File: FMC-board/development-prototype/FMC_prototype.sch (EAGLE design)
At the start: 3 parts

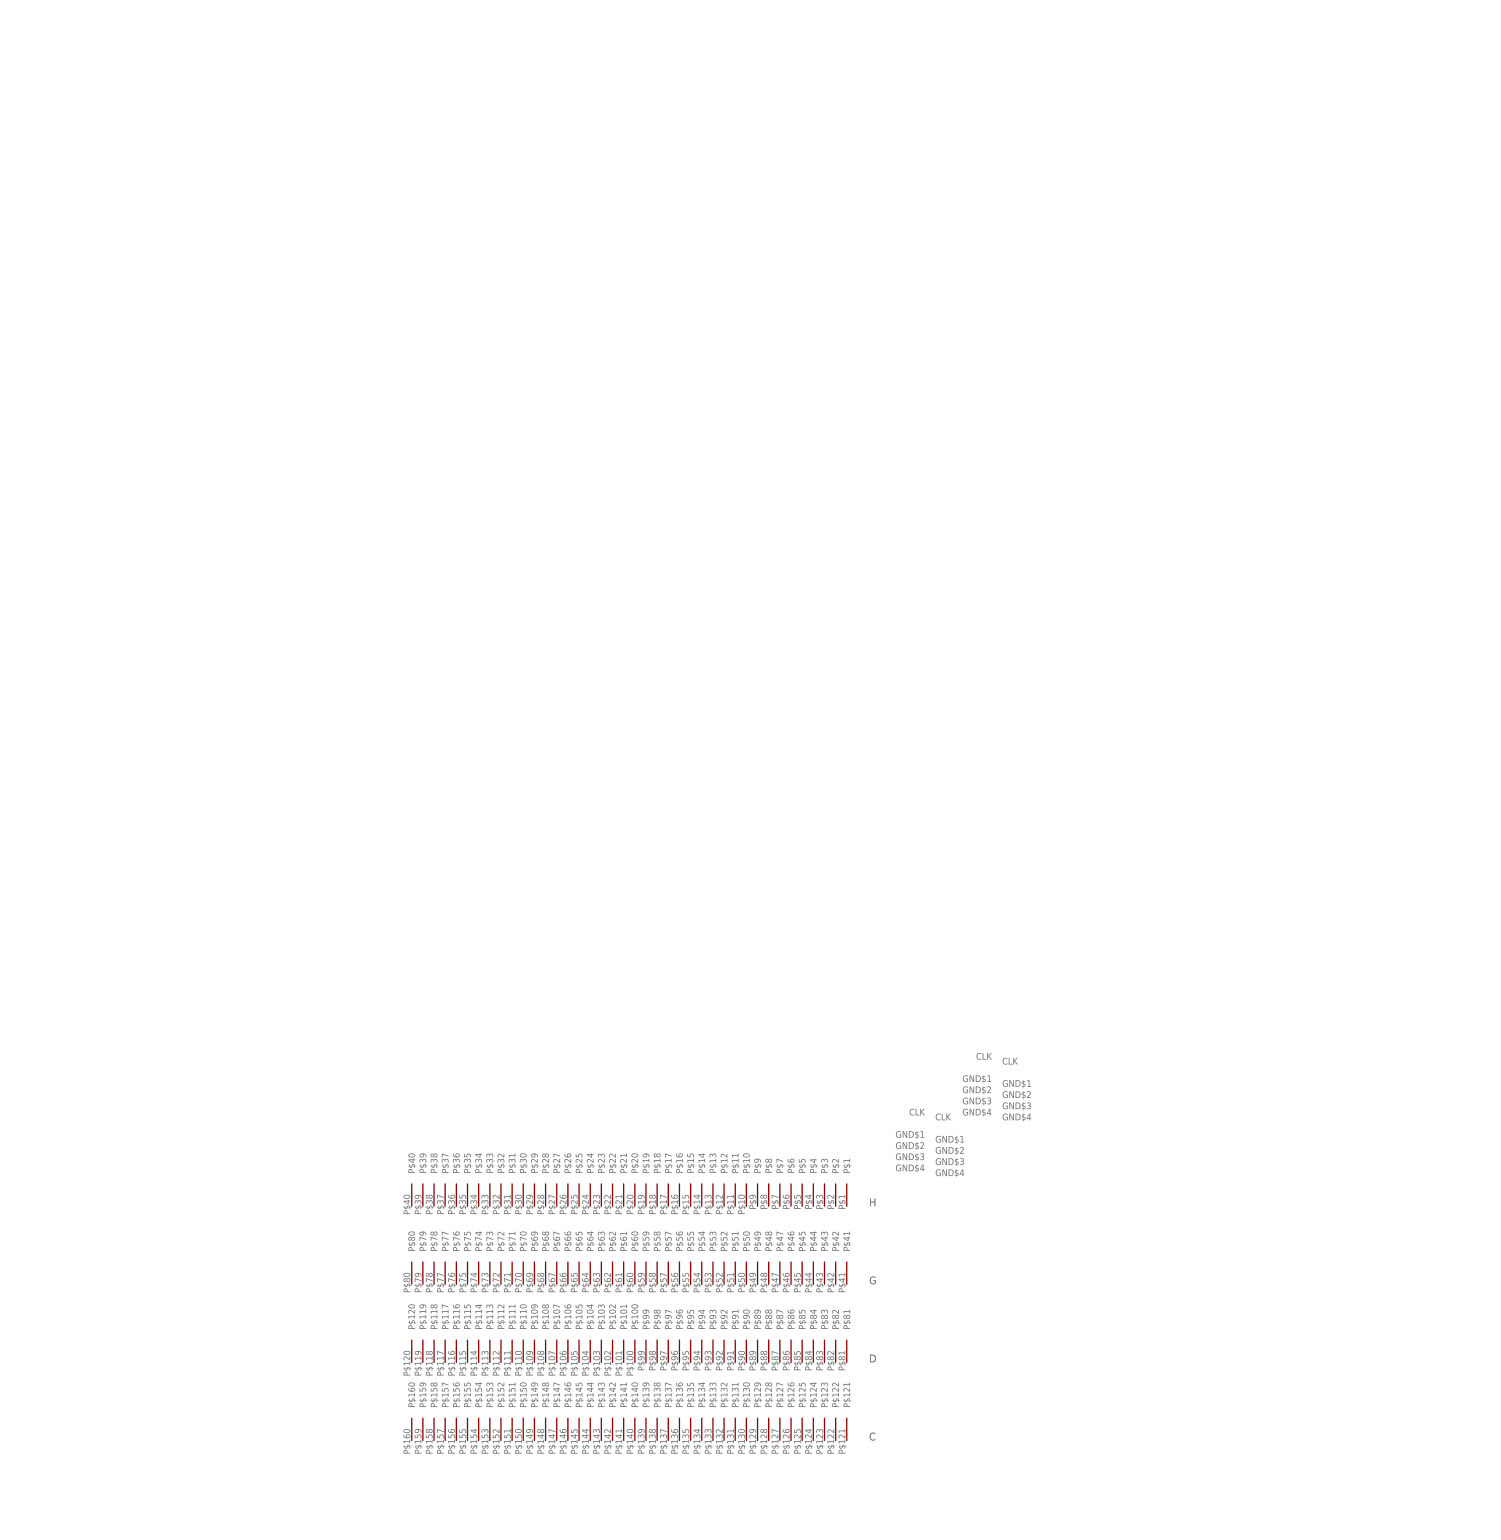
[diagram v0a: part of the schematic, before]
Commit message: added basic isolator circuitry sch
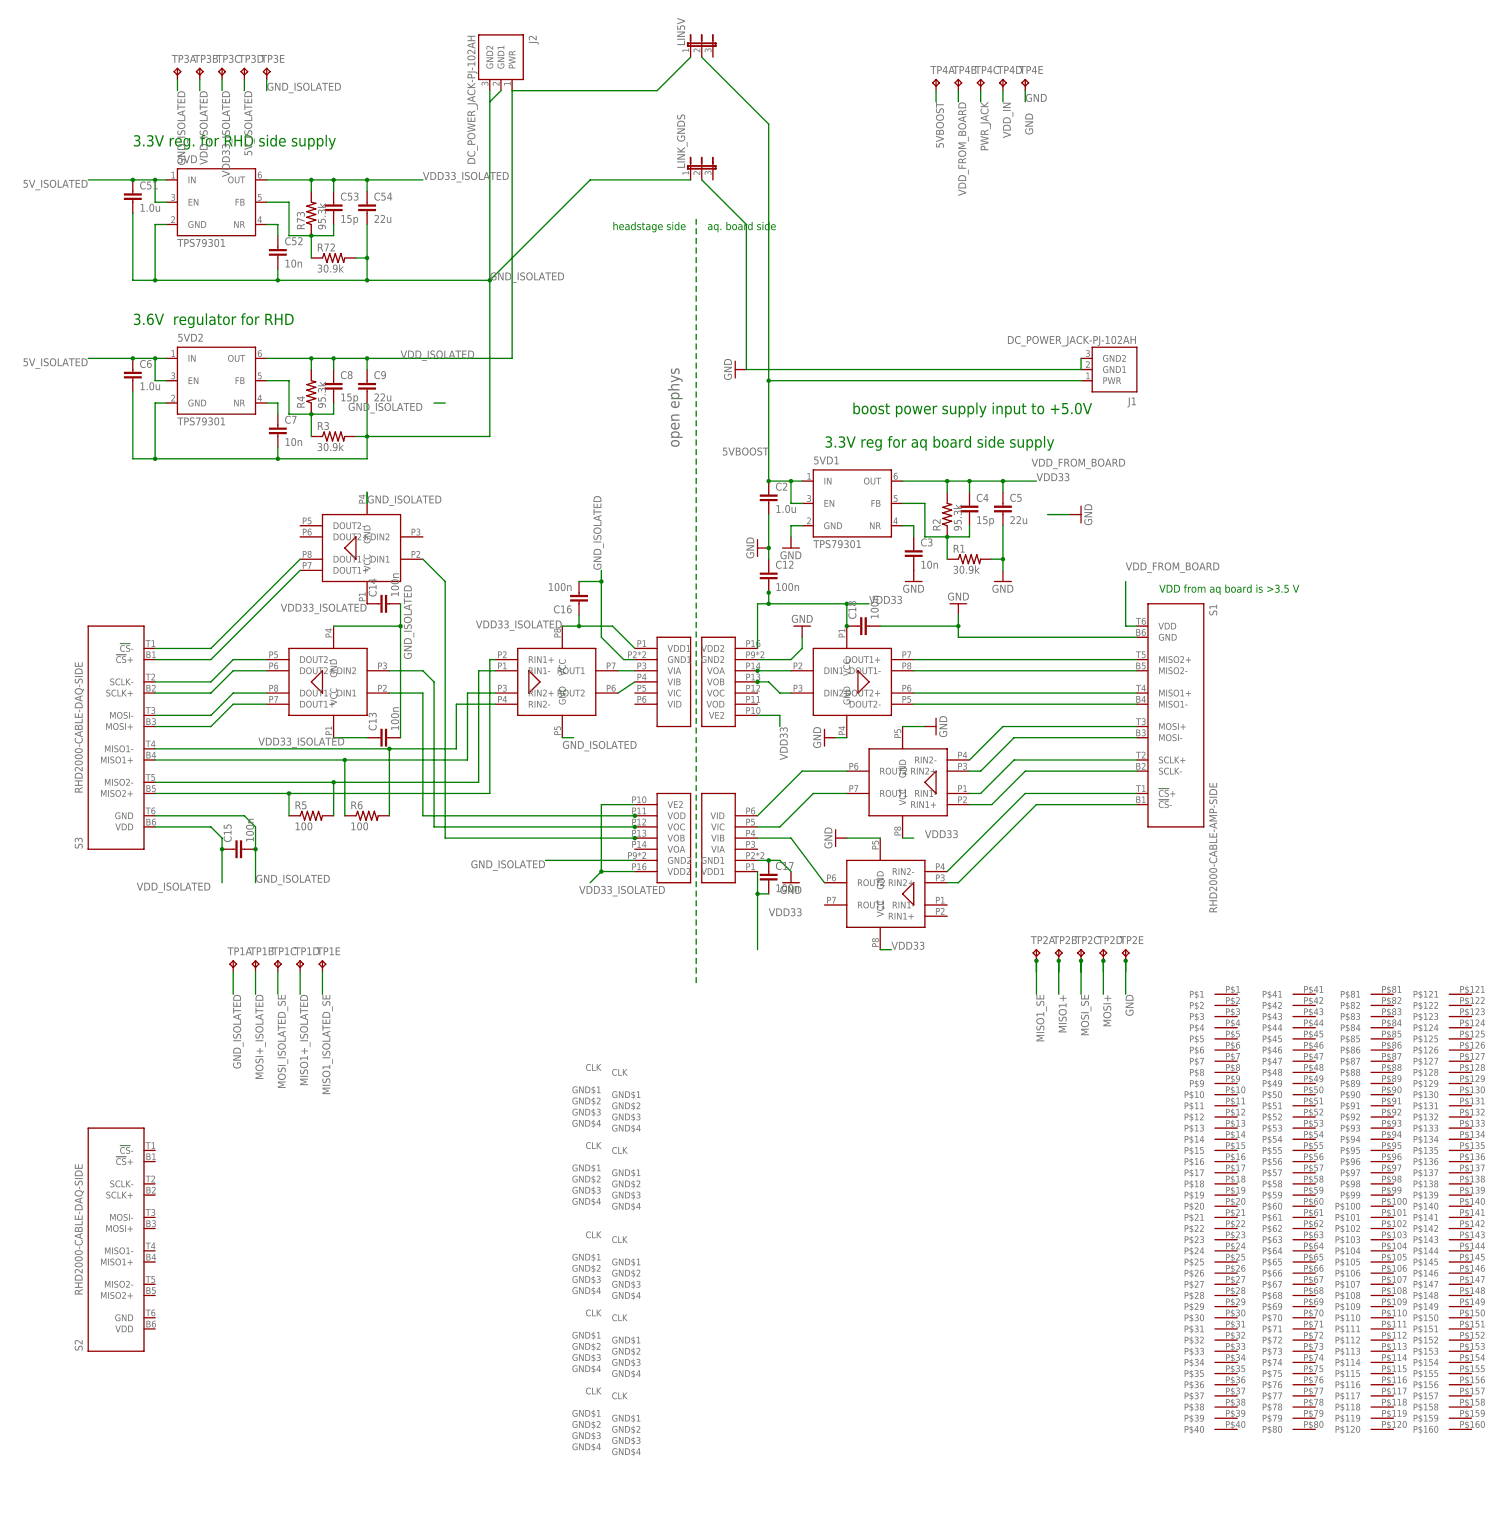
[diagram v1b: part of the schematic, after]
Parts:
- added 5VD, 5VD1, 5VD2: TPS79301, RHD2000_eval_board:TPS79301
- added C12, C13, C14, C15, C16, C17, C18: 100n, RHD2000_eval_board:C_0603
- added C2, C51, C6: 1.0u, RHD2000_eval_board:C_0805
- added C3, C52, C7: 10n, RHD2000_eval_board:C_0603
- added C4, C53, C8: 15p, RHD2000_eval_board:C_0603
- added C5, C54, C9: 22u, RHD2000_eval_board:C_1206
- added J1, J2: DC_POWER_JACK-PJ-102AH, RHD2000_eval_board:DC_POWER_JACK-PJ-102AH
- added LIN5V, LINK_GNDS: (no value), jumper:JP2E
- added R1, R3, R72: 30.9k, RHD2000_eval_board:R_0603
- added R2, R4, R73: 95.3k, RHD2000_eval_board:R_0603
- added R5, R6: 100, RHD2000_eval_board:R_0603
- added S1: RHD2000-CABLE-AMP-SIDE, RHD2000:RHD2000-CABLE-AMP-SIDE
- added S2, S3: RHD2000-CABLE-DAQ-SIDE, RHD2000_eval_board:RHD2000-CABLE-DAQ-SIDE
- added TP1, TP2, TP3, TP4: TP5P5-25-13, testpad:TP5P5-25-13
- added U$1: OPEN_EPHYS_LOGO, open-ephys:OPEN_EPHYS_LOGO
- added U$10, U$6, U$8: ADN4664, open-ephys:ADN4664
- added U$11, U$12: ADUM3440, open-ephys_old:ADUM3440
- added U$13, U$14, U$15: SMA_JACK_142-0701-201_DEV, SA_BB:SMA_JACK_142-0701-201_DEV
- added U$3, U$7, U$9: ADN4663, open-ephys:ADN4663
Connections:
- new net 5VBOOST: 5VD1.EN, 5VD1.IN, C2.1, J1.PWR, LIN5V.2, TP4A.TP
- new net 5V_ISOLATED: 5VD.EN, 5VD.IN, 5VD2.EN, 5VD2.IN, C51.1, C6.1, TP3D.TP
- new net CS+: S1.!CS!+, U$10.RIN2-
- new net CS+_ISOLATED: S3.!CS!+, U$9.DOUT1+
- new net CS-: S1.!CS!-, U$10.RIN2+
- new net CS-_ISOLATED: S3.!CS!-, U$9.DOUT1-
- new net CS_ISOLATED_SE: U$12.VOB, U$9.DIN1
- new net CS_SE: U$10.ROUT2, U$12.VIB
- new net GND: 5VD1.GND, C12.1, C17.1, C18.2, C2.2, C3.2, C5.2, J1.GND1, J1.GND2, LINK_GNDS.2, R1.2, S1.GND, TP2E.TP, TP4E.TP, U$10.GND, U$11.GND2, U$12.GND1, U$3.GND, U$8.GND
- new net GND4: C15.2
- new net GND_ISOLATED: 5VD.GND, 5VD2.GND, C13.2, C14.2, C16.2, C51.2, C52.2, C54.2, C6.2, C7.2, C9.2, J2.GND1, J2.GND2, LINK_GNDS.1, R3.2, R72.2, S3.GND, TP1A.TP, TP3A.TP, TP3E.TP, U$11.GND1, U$12.GND2, U$6.GND, U$7.GND, U$9.GND
- new net MISO1+: S1.MISO1+, TP2B.TP, U$3.DOUT2+
- new net MISO1+_ISOLATED: R6.1, S3.MISO1+, TP1D.TP, U$6.RIN2+
- new net MISO1-: S1.MISO1-, U$3.DOUT2-
- new net MISO1-_ISOLATED: R6.2, S3.MISO1-, U$6.RIN2-
- new net MISO1_ISOLATED_SE: TP1E.TP, U$11.VIB, U$6.ROUT2
- new net MISO1_SE: TP2A.TP, U$11.VOB, U$3.DIN2
- new net MISO2+: S1.MISO2+, U$3.DOUT1+
- new net MISO2+_ISOLATED: R5.1, S3.MISO2+, U$6.RIN1+
- new net MISO2-: S1.MISO2-, U$3.DOUT1-
- new net MISO2-_ISOLATED: R5.2, S3.MISO2-, U$6.RIN1-
- new net MISO2_ISOLATED_SE: U$11.VIA, U$6.ROUT1
- new net MISO2_SE: U$11.VOA, U$3.DIN1
- new net MOSI+: S1.MOSI+, TP2D.TP, U$8.RIN2-
- new net MOSI+_ISOLATED: S3.MOSI+, TP1B.TP, U$7.DOUT1+
- new net MOSI-: S1.MOSI-, U$8.RIN2+
- new net MOSI-_ISOLATED: S3.MOSI-, U$7.DOUT1-
- new net MOSI_ISOLATED_SE: TP1C.TP, U$12.VOD, U$7.DIN1
- new net MOSI_SE: TP2C.TP, U$12.VID, U$8.ROUT2
- new net N$108: 5VD.FB, C53.2, R72.1, R73.1
- new net N$33: 5VD1.NR, C3.1
- new net N$35: 5VD1.FB, C4.2, R1.1, R2.1
- new net N$36: 5VD2.NR, C7.1
- new net N$37: 5VD2.FB, C8.2, R3.1, R4.1
- new net N$97: 5VD.NR, C52.1
- new net PWR_JACK: TP4C.TP
- new net SCLK+: S1.SCLK+, U$8.RIN1-
- new net SCLK+_ISOLATED: S3.SCLK+, U$7.DOUT2+
- new net SCLK-: S1.SCLK-, U$8.RIN1+
- new net SCLK-_ISOLATED: S3.SCLK-, U$7.DOUT2-
- new net SCLK_ISOLATED_SE: U$12.VOC, U$7.DIN2
- new net SCLK_SE: U$12.VIC, U$8.ROUT1
- new net VDD33: 5VD1.OUT, C12.2, C17.2, C18.1, C4.1, C5.1, R2.2, U$10.VCC, U$11.VDD2, U$11.VE2, U$12.VDD1, U$3.VCC, U$8.VCC
- new net VDD33_ISOLATED: 5VD.OUT, C13.1, C14.1, C16.1, C53.1, C54.1, R73.2, TP3C.TP, U$11.VDD1, U$12.VDD2, U$12.VE2, U$6.VCC, U$7.VCC, U$9.VCC
- new net VDD_FROM_BOARD: S1.VDD, TP4B.TP
- new net VDD_IN: TP4D.TP
- new net VDD_ISOLATED: 5VD2.OUT, C15.1, C8.1, C9.1, J2.PWR, LIN5V.1, R4.2, S3.VDD, TP3B.TP
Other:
- note added: "3.3V reg for aq board side supply"
- note added: "3.3V reg. for RHD side supply"
- note added: "3.6V regulator for RHD"
- note added: "VDD from aq board is >3.5 V"
- note added: "aq. board side"
- note added: "boost power supply input to +5.0V"
- note added: "headstage side"
- note removed: "C"
- note removed: "D"
- note removed: "G"
- note removed: "H"
